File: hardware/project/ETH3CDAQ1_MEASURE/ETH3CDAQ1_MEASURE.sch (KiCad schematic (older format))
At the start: 2 parts

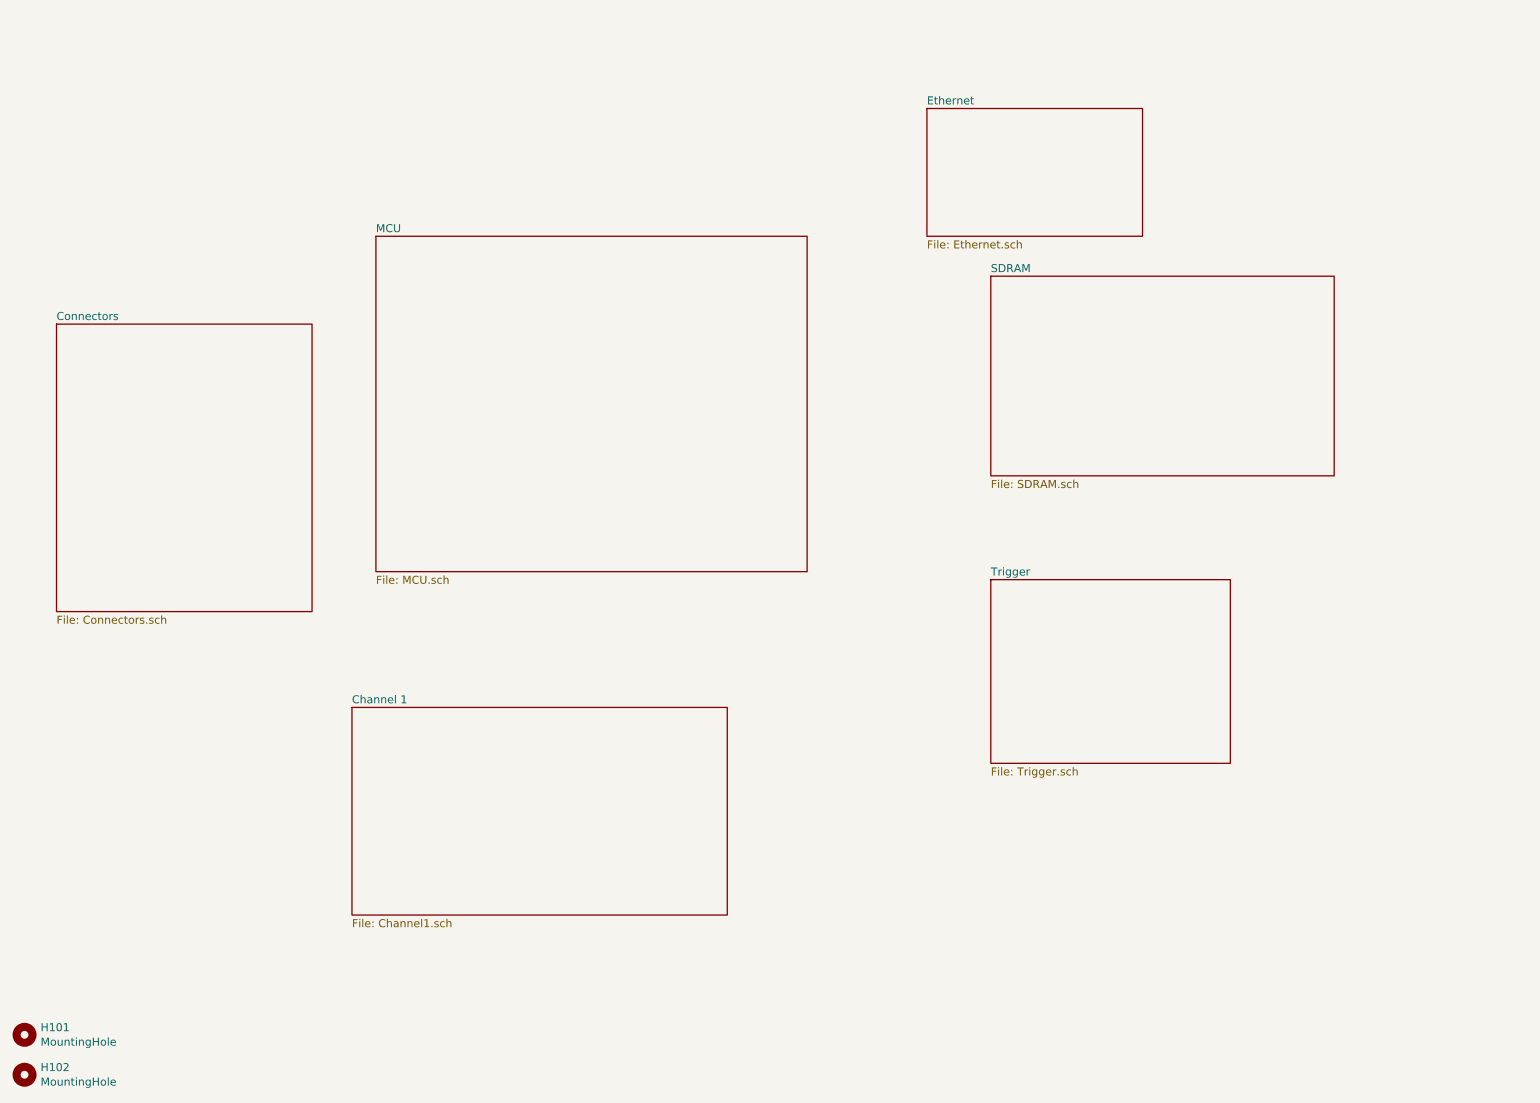
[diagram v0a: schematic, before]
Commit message: Meas. module schematic design.
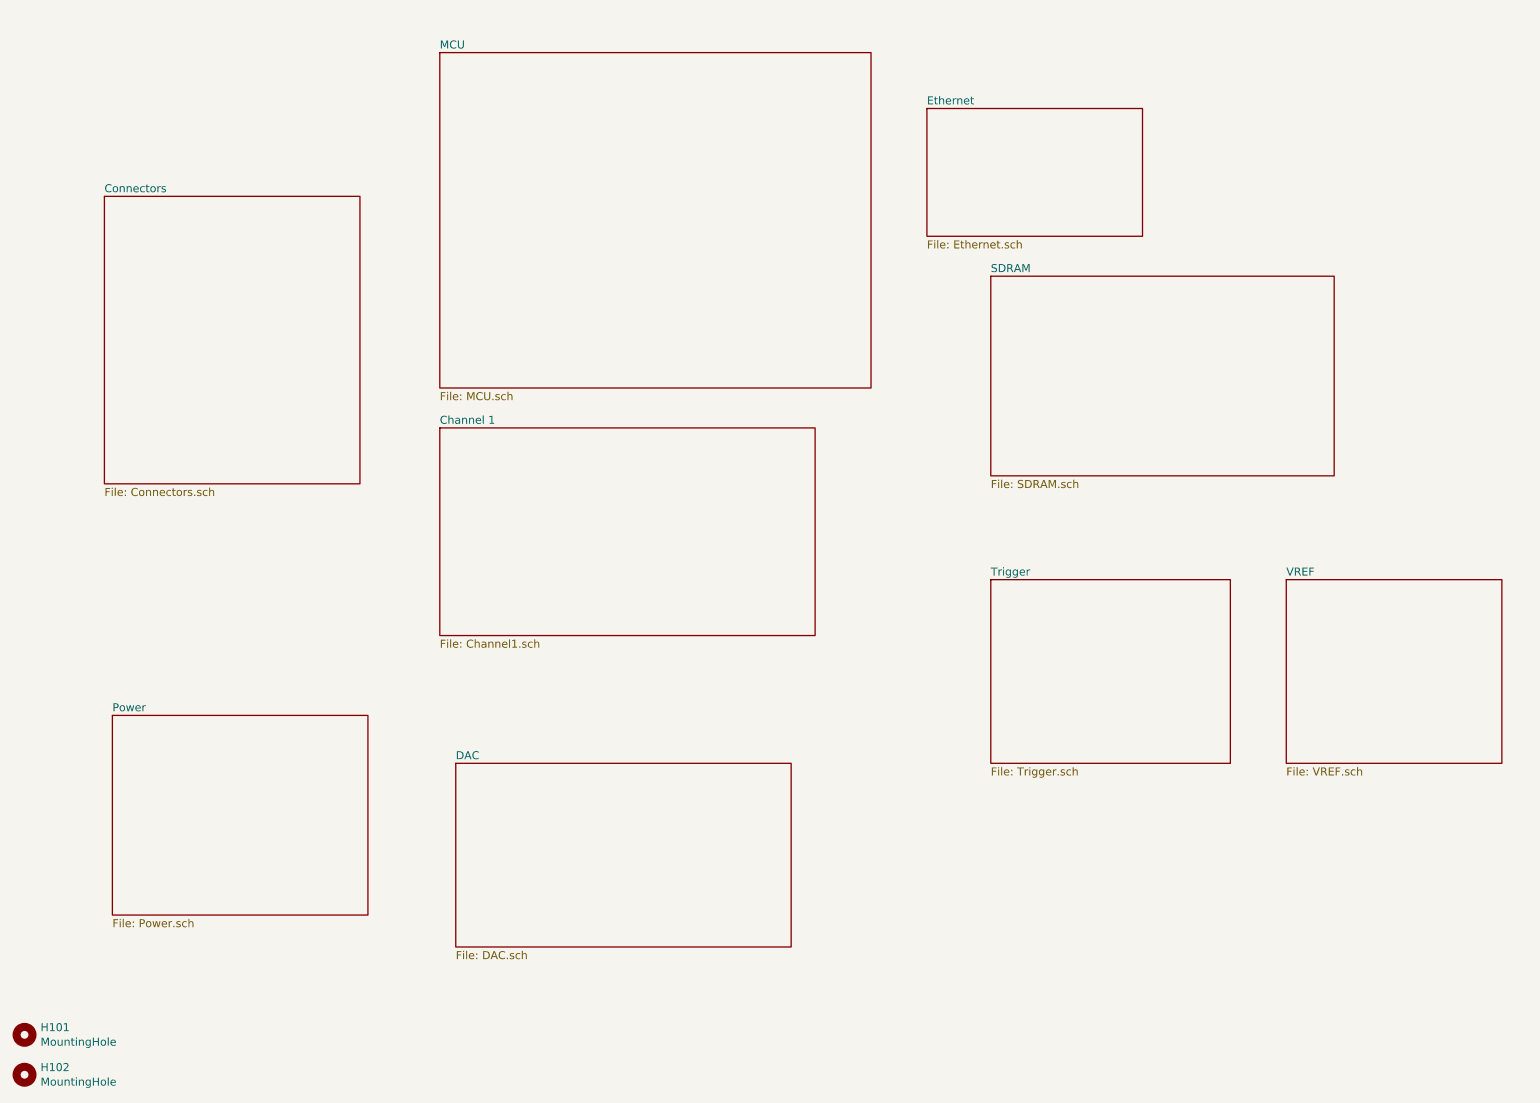
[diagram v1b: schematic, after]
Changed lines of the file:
@@
 $Descr A4 11693 8268
 encoding utf-8
-Sheet 1 7
+Sheet 1 10
 Title ""
 Date ""
@@
 $EndDescr
 $Sheet
-S 3250 2050 2700 2100
+S 3650 900  2700 2100
 U 5FB582AF
 F0 "MCU" 50
@@
 $EndSheet
 $Sheet
-S 3100 5000 2350 1300
+S 3650 3250 2350 1300
 U 5FB85416
 F0 "Channel 1" 50
@@
 $EndSheet
 $Sheet
-S 1250 2600 1600 1800
+S 1550 1800 1600 1800
 U 5FC84995
 F0 "Connectors" 50
 F1 "Connectors.sch" 50
 $EndSheet
+$Sheet
+S 8950 4200 1350 1150
+U 5FC8249B
+F0 "VREF" 50
+F1 "VREF.sch" 50
+$EndSheet
+$Sheet
+S 3750 5350 2100 1150
+U 5FB6952A
+F0 "DAC" 50
+F1 "DAC.sch" 50
+$EndSheet
+$Sheet
+S 1600 5050 1600 1250
+U 5FED0BD8
+F0 "Power" 50
+F1 "Power.sch" 50
+$EndSheet
 $EndSCHEMATC

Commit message: PCB design
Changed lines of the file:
@@
 F0 "Channel 3" 50
 F1 "Channel3.sch" 50
+F2 "DAC_V3" I L 5500 3300 50
+F3 "CH3_IN" I L 5500 3200 50
+F4 "SR3_CLK" B R 6550 3400 50
+F5 "SR3_LAT" B R 6550 3300 50
+F6 "ADC3_~CS" B R 6550 3600 50
+F7 "ADC3_SCLK" B R 6550 3700 50
+F8 "ADC3_SDI" B R 6550 3800 50
+F9 "ADC3_SDO" B R 6550 3900 50
+F10 "SR2_QH" B R 6550 3200 50
 $EndSheet
+Wire Wire Line
+	5500 3200 5050 3200
+Wire Wire Line
+	5500 4400 5400 4400
+Wire Wire Line
+	5400 4400 5400 3300
+Wire Wire Line
+	5400 3300 5500 3300
+Wire Wire Line
+	6550 3600 6900 3600
+Wire Wire Line
+	6900 3600 6900 2450
+Connection ~ 6900 2450
+Wire Wire Line
+	6550 3700 6950 3700
+Wire Wire Line
+	6950 3700 6950 2550
+Connection ~ 6950 2550
+Wire Wire Line
+	6550 2750 6700 2750
+Wire Wire Line
+	6700 2750 6700 3800
+Wire Wire Line
+	6700 3800 6550 3800
+Wire Wire Line
+	6550 3900 7000 3900
+Wire Wire Line
+	7000 3900 7000 1600
+Wire Wire Line
+	7000 1600 7050 1600
+Wire Wire Line
+	6550 3400 6800 3400
+Wire Wire Line
+	6800 3400 6800 2250
+Connection ~ 6800 2250
+Wire Wire Line
+	6550 3300 6750 3300
+Wire Wire Line
+	6750 3300 6750 2150
+Connection ~ 6750 2150
+Wire Wire Line
+	6550 3200 6650 3200
+Wire Wire Line
+	6650 3200 6650 2350
+Wire Wire Line
+	6650 2350 6550 2350
 $EndSCHEMATC

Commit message: PCB design
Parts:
- H101, H102: footprint MountingHole:MountingHole_2.7mm_M2.5_DIN965_Pad -> MountingHole:MountingHole_3.2mm_M3_DIN965_Pad
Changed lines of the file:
@@
 F 0 "H101" H 1150 7096 50  0000 L CNN
 F 1 "MountingHole" H 1150 7005 50  0000 L CNN
-F 2 "MountingHole:MountingHole_2.7mm_M2.5_DIN965_Pad" H 1050 7050 50  0001 C CNN
+F 2 "MountingHole:MountingHole_3.2mm_M3_DIN965_Pad" H 1050 7050 50  0001 C CNN
 F 3 "~" H 1050 7050 50  0001 C CNN
 	1    1050 7050
@@
 F 0 "H102" H 1150 7346 50  0000 L CNN
 F 1 "MountingHole" H 1150 7255 50  0000 L CNN
-F 2 "MountingHole:MountingHole_2.7mm_M2.5_DIN965_Pad" H 1050 7300 50  0001 C CNN
+F 2 "MountingHole:MountingHole_3.2mm_M3_DIN965_Pad" H 1050 7300 50  0001 C CNN
 F 3 "~" H 1050 7300 50  0001 C CNN
 	1    1050 7300

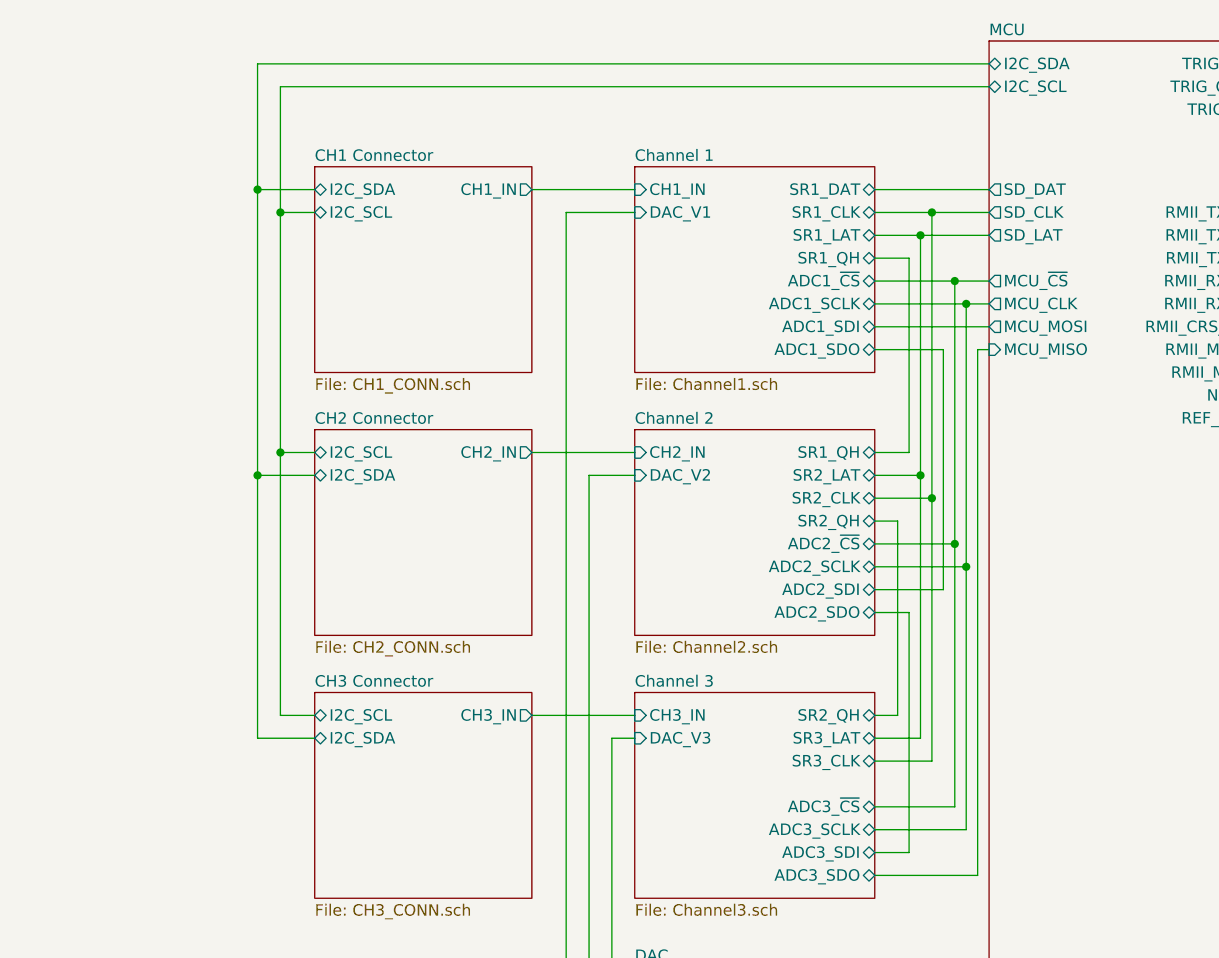
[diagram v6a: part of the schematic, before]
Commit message: Started development of first current measurement module. Added CAN to the DAQ module.
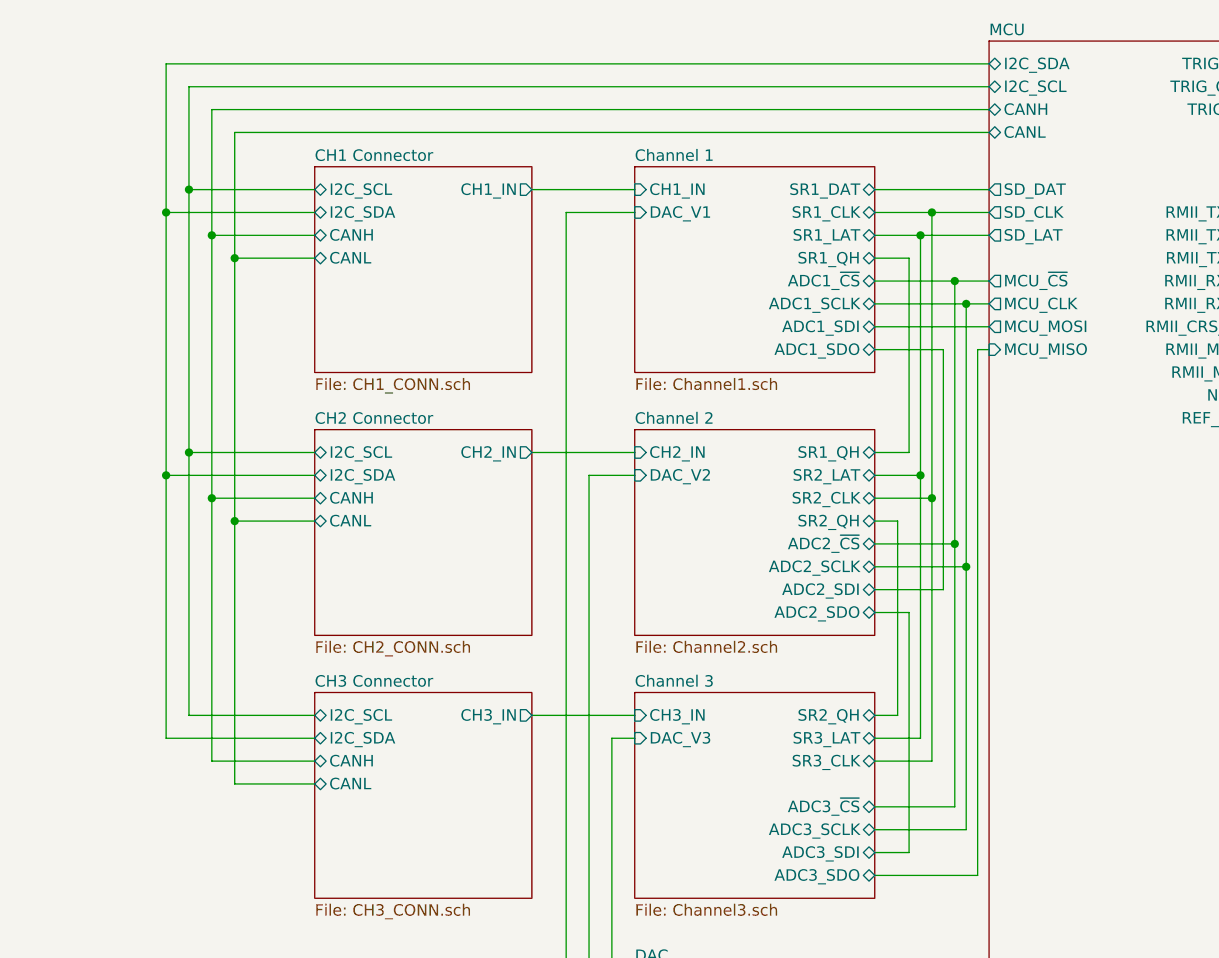
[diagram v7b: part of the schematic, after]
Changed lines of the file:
@@
 F38 "I2C_SCL" B L 5600 950 50
 F39 "I2C_SDA" B L 5600 850 50
+F40 "CANH" B L 5600 1050 50
+F41 "CANL" B L 5600 1150 50
 $EndSheet
 $Comp
@@
 Wire Wire Line
 	5200 3700 5200 2850
-Connection ~ 2500 2550
-Wire Wire Line
-	2500 1500 2650 1500
-Wire Wire Line
-	2500 2550 2500 1500
-Wire Wire Line
-	2500 2550 2650 2550
-Wire Wire Line
-	2500 3700 2500 2550
-Wire Wire Line
-	2650 3700 2500 3700
-Connection ~ 2400 2650
-Wire Wire Line
-	2400 3800 2650 3800
-Wire Wire Line
-	2400 2650 2400 3800
-Wire Wire Line
-	2400 2650 2650 2650
-Wire Wire Line
-	2400 1400 2400 2650
-Wire Wire Line
-	2650 1400 2400 1400
 Wire Wire Line
 	5200 2850 5100 2850
@@
 F3 "I2C_SDA" B L 2650 3800 50
 F4 "CH3_IN" O R 3600 3700 50
+F5 "CANH" B L 2650 3900 50
+F6 "CANL" B L 2650 4000 50
 $EndSheet
 $Sheet
@@
 F3 "I2C_SDA" B L 2650 2650 50
 F4 "CH2_IN" O R 3600 2550 50
+F5 "CANH" B L 2650 2750 50
+F6 "CANL" B L 2650 2850 50
 $EndSheet
 Wire Wire Line
@@
 F0 "CH1 Connector" 50
 F1 "CH1_CONN.sch" 50
-F2 "I2C_SCL" B L 2650 1500 50
-F3 "I2C_SDA" B L 2650 1400 50
+F2 "I2C_SCL" B L 2650 1400 50
+F3 "I2C_SDA" B L 2650 1500 50
 F4 "CH1_IN" O R 3600 1400 50
+F5 "CANH" B L 2650 1600 50
+F6 "CANL" B L 2650 1700 50
 $EndSheet
 Wire Wire Line
@@
 	5100 4900 5600 4900
 Wire Wire Line
-	5600 850  2400 850
-Wire Wire Line
-	2400 850  2400 1400
-Connection ~ 2400 1400
-Wire Wire Line
-	5600 950  2500 950
-Wire Wire Line
-	2500 950  2500 1500
-Connection ~ 2500 1500
+	2650 3800 2000 3800
+Wire Wire Line
+	2000 3800 2000 2650
+Wire Wire Line
+	2000 2650 2650 2650
+Wire Wire Line
+	2000 2650 2000 1500
+Wire Wire Line
+	2000 1500 2650 1500
+Connection ~ 2000 2650
+Wire Wire Line
+	2650 3700 2100 3700
+Wire Wire Line
+	2100 3700 2100 2550
+Wire Wire Line
+	2100 1400 2650 1400
+Wire Wire Line
+	2650 2550 2100 2550
+Connection ~ 2100 2550
+Wire Wire Line
+	2100 2550 2100 1400
+Wire Wire Line
+	2100 1400 2100 950
+Wire Wire Line
+	2100 950  5600 950
+Connection ~ 2100 1400
+Wire Wire Line
+	2000 1500 2000 850
+Wire Wire Line
+	2000 850  5600 850
+Connection ~ 2000 1500
+Wire Wire Line
+	5600 1050 2200 1050
+Wire Wire Line
+	2200 1050 2200 1600
+Wire Wire Line
+	2200 1600 2650 1600
+Wire Wire Line
+	2200 1600 2200 2750
+Wire Wire Line
+	2200 2750 2650 2750
+Connection ~ 2200 1600
+Wire Wire Line
+	2200 2750 2200 3900
+Wire Wire Line
+	2200 3900 2650 3900
+Connection ~ 2200 2750
+Wire Wire Line
+	5600 1150 2300 1150
+Wire Wire Line
+	2300 1150 2300 1700
+Wire Wire Line
+	2300 1700 2650 1700
+Wire Wire Line
+	2300 1700 2300 2850
+Wire Wire Line
+	2300 2850 2650 2850
+Connection ~ 2300 1700
+Wire Wire Line
+	2300 2850 2300 4000
+Wire Wire Line
+	2300 4000 2650 4000
+Connection ~ 2300 2850
 $EndSCHEMATC

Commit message: Modification in PCBs. Created BOM files.
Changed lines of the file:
@@
 F22 "~RAS" B L 5600 6550 50
 F23 "D[0..15]" B L 5600 6750 50
-F24 "A[0..11]" B L 5600 6650 50
-F25 "BA0" B L 5600 5650 50
-F26 "BA1" B L 5600 5750 50
-F27 "SD_DAT" O L 5600 1400 50
-F28 "SD_CLK" O L 5600 1500 50
-F29 "SD_LAT" O L 5600 1600 50
-F30 "MCU_CLK" O L 5600 1900 50
-F31 "MCU_MISO" I L 5600 2100 50
-F32 "MCU_~CS" O L 5600 1800 50
-F33 "MCU_MOSI" O L 5600 2000 50
-F34 "DAC_~SYNC" O L 5600 4900 50
-F35 "DAC_DIN" O L 5600 5000 50
-F36 "DAC_SCLK" O L 5600 5100 50
-F37 "DAC_LDAC" O L 5600 5200 50
-F38 "I2C_SCL" B L 5600 950 50
-F39 "I2C_SDA" B L 5600 850 50
-F40 "CANH" B L 5600 1050 50
-F41 "CANL" B L 5600 1150 50
+F24 "BA0" B L 5600 5650 50
+F25 "BA1" B L 5600 5750 50
+F26 "SD_DAT" O L 5600 1400 50
+F27 "SD_CLK" O L 5600 1500 50
+F28 "SD_LAT" O L 5600 1600 50
+F29 "MCU_CLK" O L 5600 1900 50
+F30 "MCU_MISO" I L 5600 2100 50
+F31 "MCU_~CS" O L 5600 1800 50
+F32 "MCU_MOSI" O L 5600 2000 50
+F33 "DAC_~SYNC" O L 5600 4900 50
+F34 "DAC_DIN" O L 5600 5000 50
+F35 "DAC_SCLK" O L 5600 5100 50
+F36 "DAC_LDAC" O L 5600 5200 50
+F37 "I2C_SCL" B L 5600 950 50
+F38 "I2C_SDA" B L 5600 850 50
+F39 "CANH" B L 5600 1050 50
+F40 "CANL" B L 5600 1150 50
+F41 "A[0..12]" B L 5600 6650 50
 $EndSheet
 $Comp
@@
 $EndSheet
 $Sheet
-S 6950 4250 950  2050
+S 6950 4100 950  2050
 U 5FED0BD8
 F0 "Power" 50
@@
 F10 "~CAS" B R 5100 6450 50
 F11 "~RAS" B R 5100 6550 50
-F12 "A[0..11]" B R 5100 6650 50
-F13 "D[0..15]" B R 5100 6750 50
-$EndSheet
-$Sheet
+F12 "D[0..15]" B R 5100 6750 50
+F13 "A[0..12]" B R 5100 6650 50
+$EndSheet
+$Sheet
